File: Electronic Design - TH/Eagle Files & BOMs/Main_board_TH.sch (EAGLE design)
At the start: 41 parts, among them M1 ARDUINO-NANO-3.0, Q1 IRF9520, Q2 IRF9520

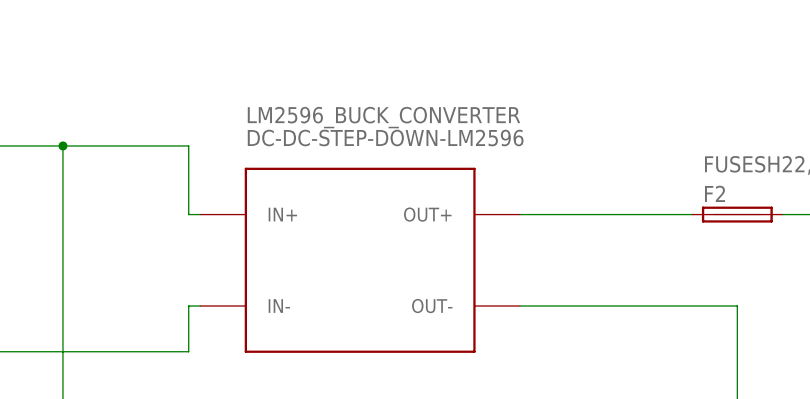
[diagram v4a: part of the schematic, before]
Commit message: Redoing names of sections so that they fit and adding in versioning and a place for people to put their names
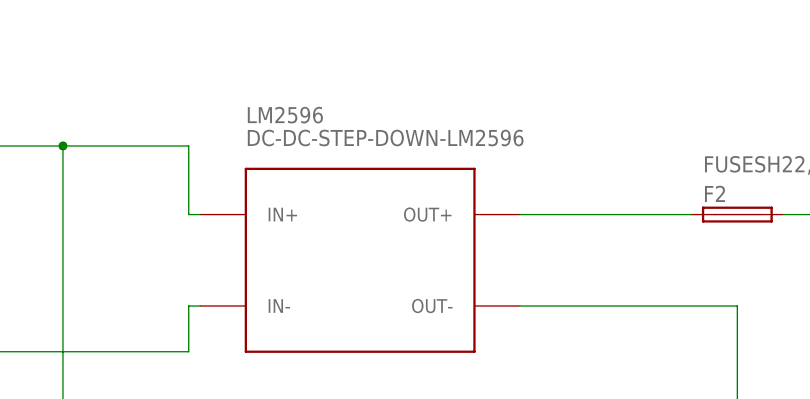
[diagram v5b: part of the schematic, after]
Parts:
- renumbered LM2596_BUCK_CONVERTER to LM2596
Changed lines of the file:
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@@
 <setting verticaltext="up"/>
 </settings>
-<grid distance="0.05" unitdist="inch" unit="inch" style="lines" multiple="1" display="no" altdistance="0.01" altunitdist="inch" altunit="inch"/>
+<grid distance="0.1" unitdist="inch" unit="inch" style="lines" multiple="1" display="no" altdistance="0.01" altunitdist="inch" altunit="inch"/>
 <layers>
 <layer number="1" name="Top" color="4" fill="1" visible="no" active="no"/>
@@
 <part name="Q2" library="Samson" deviceset="PMOSFET_P" device="TO220BV" value="IRF9520"/>
 <part name="F1" library="fuse" deviceset="FUSE" device="SH22,5A" value="FUSESH22,5A"/>
-<part name="LM2596_BUCK_CONVERTER" library="diy-modules" deviceset="DC-DC-STEP-DOWN-LM2596" device=""/>
+<part name="LM2596" library="diy-modules" deviceset="DC-DC-STEP-DOWN-LM2596" device=""/>
 <part name="SUPPLY9" library="supply2" deviceset="GND" device=""/>
 <part name="M1" library="diy-modules" deviceset="ARDUINO-NANO-3.0" device=""/>
@@
 <attribute name="VALUE" x="-96.52" y="93.599" size="1.778" layer="96"/>
 </instance>
-<instance part="LM2596_BUCK_CONVERTER" gate="G$1" x="101.6" y="76.2"/>
+<instance part="LM2596" gate="G$1" x="101.6" y="76.2"/>
 <instance part="SUPPLY9" gate="GND" x="-5.08" y="63.5"/>
 <instance part="M1" gate="G$1" x="-77.47" y="21.59"/>
@@
 <wire x1="68.58" y1="88.9" x2="82.55" y2="88.9" width="0.1524" layer="91"/>
 <wire x1="82.55" y1="88.9" x2="82.55" y2="81.28" width="0.1524" layer="91"/>
-<pinref part="LM2596_BUCK_CONVERTER" gate="G$1" pin="IN+"/>
+<pinref part="LM2596" gate="G$1" pin="IN+"/>
 <wire x1="82.55" y1="81.28" x2="83.82" y2="81.28" width="0.1524" layer="91"/>
 <junction x="68.58" y="88.9"/>
@@
 <segment>
 <pinref part="F2" gate="G$1" pin="1"/>
-<pinref part="LM2596_BUCK_CONVERTER" gate="G$1" pin="OUT+"/>
+<pinref part="LM2596" gate="G$1" pin="OUT+"/>
 <wire x1="119.38" y1="81.28" x2="138.43" y2="81.28" width="0.1524" layer="91"/>
 </segment>
@@
 <net name="N$4" class="0">
 <segment>
-<pinref part="LM2596_BUCK_CONVERTER" gate="G$1" pin="IN-"/>
+<pinref part="LM2596" gate="G$1" pin="IN-"/>
 <wire x1="82.55" y1="71.12" x2="83.82" y2="71.12" width="0.1524" layer="91"/>
 <wire x1="82.55" y1="66.04" x2="82.55" y2="71.12" width="0.1524" layer="91"/>
@@
 <wire x1="163.83" y1="71.12" x2="163.83" y2="59.69" width="0.1524" layer="91"/>
 <junction x="163.83" y="59.69"/>
-<pinref part="LM2596_BUCK_CONVERTER" gate="G$1" pin="OUT-"/>
+<pinref part="LM2596" gate="G$1" pin="OUT-"/>
 <wire x1="119.38" y1="71.12" x2="143.51" y2="71.12" width="0.1524" layer="91"/>
 <wire x1="143.51" y1="71.12" x2="143.51" y2="59.69" width="0.1524" layer="91"/>

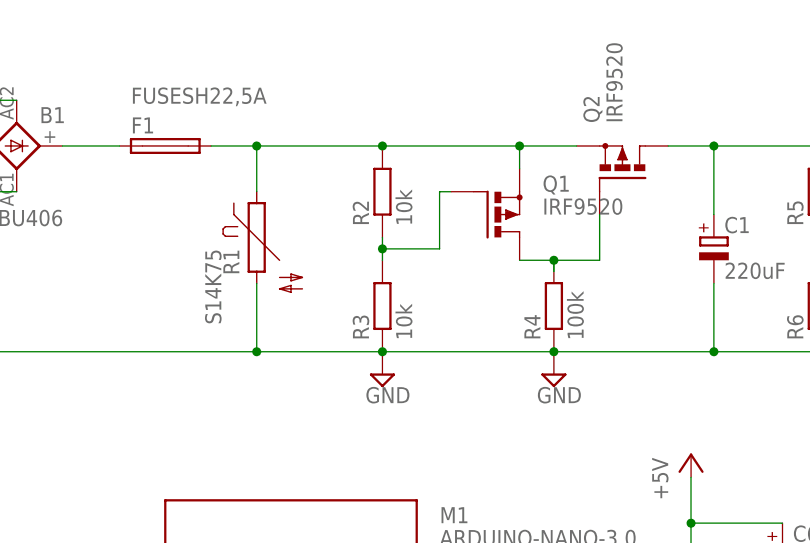
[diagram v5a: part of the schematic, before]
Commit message: updating values of divider on Q1
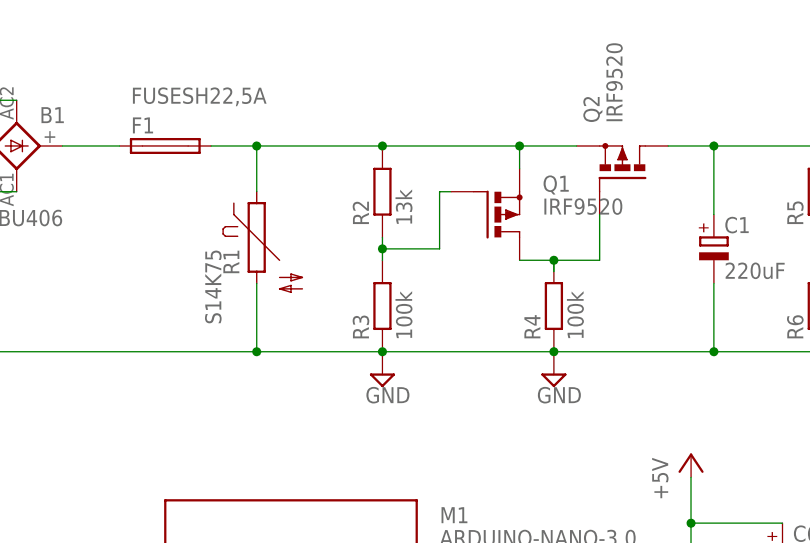
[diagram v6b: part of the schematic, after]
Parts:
- R2: value 10k -> 13k
- R3: value 10k -> 100k
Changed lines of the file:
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@@
 <part name="D3" library="diode" deviceset="ZPD" device="" value="5.1V"/>
 <part name="C5" library="resistor" deviceset="C-EU" device="050-024X044" value="10n"/>
-<part name="R2" library="resistor" deviceset="R-EU_" device="0207/10" value="10k"/>
-<part name="R3" library="resistor" deviceset="R-EU_" device="0207/10" value="10k"/>
+<part name="R2" library="resistor" deviceset="R-EU_" device="0207/10" value="13k"/>
+<part name="R3" library="resistor" deviceset="R-EU_" device="0207/10" value="100k"/>
 <part name="USB_1" library="con-berg" deviceset="PN87520-S" device=""/>
 <part name="USB_2" library="con-berg" deviceset="PN87520-S" device=""/>

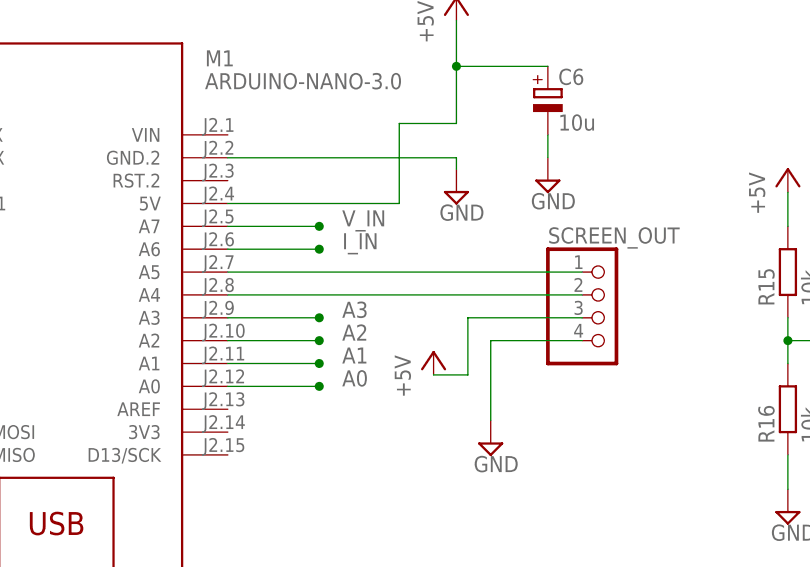
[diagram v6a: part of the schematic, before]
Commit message: updating firmware and correcting screen pins
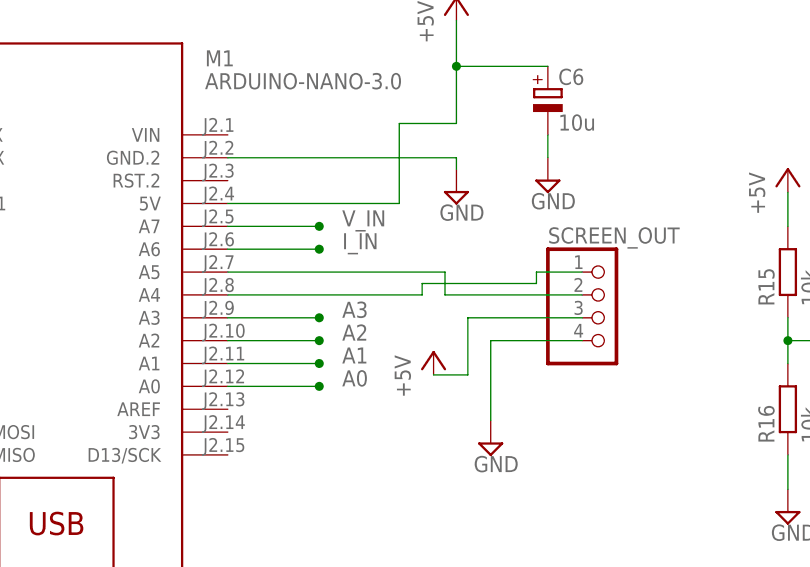
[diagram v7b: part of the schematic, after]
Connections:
- removed net A4: M1.A4, SCREEN_OUT.2
- removed net A5: M1.A5, SCREEN_OUT.1
- new net N$11: M1.A5, SCREEN_OUT.2
- new net N$12: M1.A4, SCREEN_OUT.1
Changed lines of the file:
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@@
 <setting verticaltext="up"/>
 </settings>
-<grid distance="0.1" unitdist="inch" unit="inch" style="lines" multiple="1" display="no" altdistance="0.01" altunitdist="inch" altunit="inch"/>
+<grid distance="0.05" unitdist="inch" unit="inch" style="lines" multiple="1" display="no" altdistance="0.01" altunitdist="inch" altunit="inch"/>
 <layers>
 <layer number="1" name="Top" color="4" fill="1" visible="no" active="no"/>
@@
 </segment>
 </net>
-<net name="A5" class="0">
-<segment>
-<pinref part="SCREEN_OUT" gate="A" pin="1"/>
-<pinref part="M1" gate="G$1" pin="A5"/>
-<wire x1="-20.32" y1="24.13" x2="-59.69" y2="24.13" width="0.1524" layer="91"/>
-</segment>
-</net>
-<net name="A4" class="0">
-<segment>
-<pinref part="M1" gate="G$1" pin="A4"/>
-<pinref part="SCREEN_OUT" gate="A" pin="2"/>
-<wire x1="-59.69" y1="21.59" x2="-20.32" y2="21.59" width="0.1524" layer="91"/>
-</segment>
-</net>
 <net name="N$2" class="0">
 <segment>
@@
 </segment>
 </net>
+<net name="N$11" class="0">
+<segment>
+<pinref part="M1" gate="G$1" pin="A5"/>
+<wire x1="-59.69" y1="24.13" x2="-35.56" y2="24.13" width="0.1524" layer="91"/>
+<wire x1="-35.56" y1="24.13" x2="-35.56" y2="21.59" width="0.1524" layer="91"/>
+<pinref part="SCREEN_OUT" gate="A" pin="2"/>
+<wire x1="-35.56" y1="21.59" x2="-20.32" y2="21.59" width="0.1524" layer="91"/>
+</segment>
+</net>
+<net name="N$12" class="0">
+<segment>
+<pinref part="M1" gate="G$1" pin="A4"/>
+<wire x1="-59.69" y1="21.59" x2="-38.1" y2="21.59" width="0.1524" layer="91"/>
+<wire x1="-38.1" y1="21.59" x2="-38.1" y2="22.86" width="0.1524" layer="91"/>
+<wire x1="-38.1" y1="22.86" x2="-25.4" y2="22.86" width="0.1524" layer="91"/>
+<wire x1="-25.4" y1="22.86" x2="-25.4" y2="24.13" width="0.1524" layer="91"/>
+<pinref part="SCREEN_OUT" gate="A" pin="1"/>
+<wire x1="-25.4" y1="24.13" x2="-20.32" y2="24.13" width="0.1524" layer="91"/>
+</segment>
+</net>

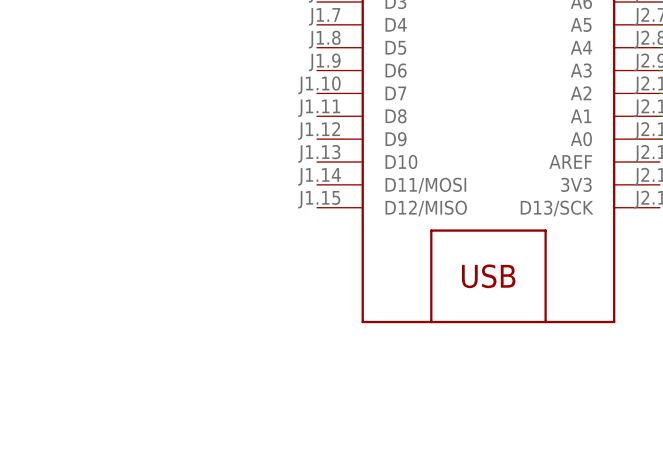
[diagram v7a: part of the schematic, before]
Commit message: adding in new LED for testing and widening board
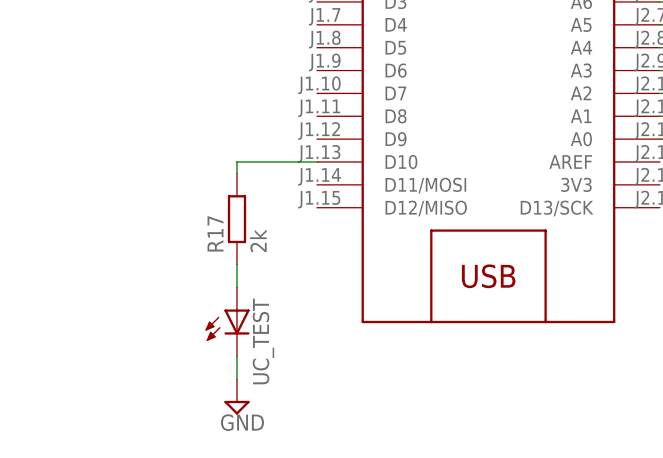
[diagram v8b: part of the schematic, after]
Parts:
- added R17: 2k, resistor:R-EU_0207/10
- added UC_TEST: (no value), led:LED3MM
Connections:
- new net N$13: M1.D10, R17.2
- new net N$14: R17.1, UC_TEST.A
- net GND: now also UC_TEST.C
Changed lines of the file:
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@@
 <part name="USB_1" library="con-berg" deviceset="PN87520-S" device=""/>
 <part name="USB_2" library="con-berg" deviceset="PN87520-S" device=""/>
+<part name="UC_TEST" library="led" deviceset="LED" device="3MM"/>
+<part name="R17" library="resistor" deviceset="R-EU_" device="0207/10" value="2k"/>
+<part name="SUPPLY2" library="supply2" deviceset="GND" device=""/>
 </parts>
 <sheets>
@@
 <instance part="USB_1" gate="G$1" x="187.96" y="62.23"/>
 <instance part="USB_2" gate="G$1" x="187.96" y="38.1"/>
+<instance part="UC_TEST" gate="G$1" x="-106.68" y="-7.62" smashed="yes">
+<attribute name="NAME" x="-103.124" y="-16.002" size="1.778" layer="95" rot="R90"/>
+<attribute name="VALUE" x="-100.965" y="-12.192" size="1.778" layer="96" rot="R90"/>
+</instance>
+<instance part="R17" gate="G$1" x="-106.68" y="2.54" rot="R90"/>
+<instance part="SUPPLY2" gate="GND" x="-106.68" y="-17.78"/>
 </instances>
 <busses>
@@
 <wire x1="-34.29" y1="36.83" x2="-34.29" y2="35.56" width="0.1524" layer="91"/>
 </segment>
+<segment>
+<pinref part="UC_TEST" gate="G$1" pin="C"/>
+<pinref part="SUPPLY2" gate="GND" pin="GND"/>
+<wire x1="-106.68" y1="-12.7" x2="-106.68" y2="-15.24" width="0.1524" layer="91"/>
+</segment>
 </net>
 <net name="VIN_PROTECTED" class="0">
@@
 </segment>
 </net>
+<net name="N$13" class="0">
+<segment>
+<pinref part="M1" gate="G$1" pin="D10"/>
+<pinref part="R17" gate="G$1" pin="2"/>
+<wire x1="-97.79" y1="8.89" x2="-106.68" y2="8.89" width="0.1524" layer="91"/>
+<wire x1="-106.68" y1="8.89" x2="-106.68" y2="7.62" width="0.1524" layer="91"/>
+</segment>
+</net>
+<net name="N$14" class="0">
+<segment>
+<pinref part="R17" gate="G$1" pin="1"/>
+<pinref part="UC_TEST" gate="G$1" pin="A"/>
+<wire x1="-106.68" y1="-2.54" x2="-106.68" y2="-5.08" width="0.1524" layer="91"/>
+</segment>
+</net>
